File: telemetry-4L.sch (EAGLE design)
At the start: 70 parts, among them SW1 MF-SW-TACT-4.2MM, SW2 PCM12SMTR, U1 ATSAMD21G18A-MUT, U2 SPX3819M5-L-3-0, U3 MCP73831T-2ACI/OT, U4 IRLML6344TRPBF, U5 SIM868, U6 BMP280, U7 MPU-9250, U8 TPS61253YFFR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

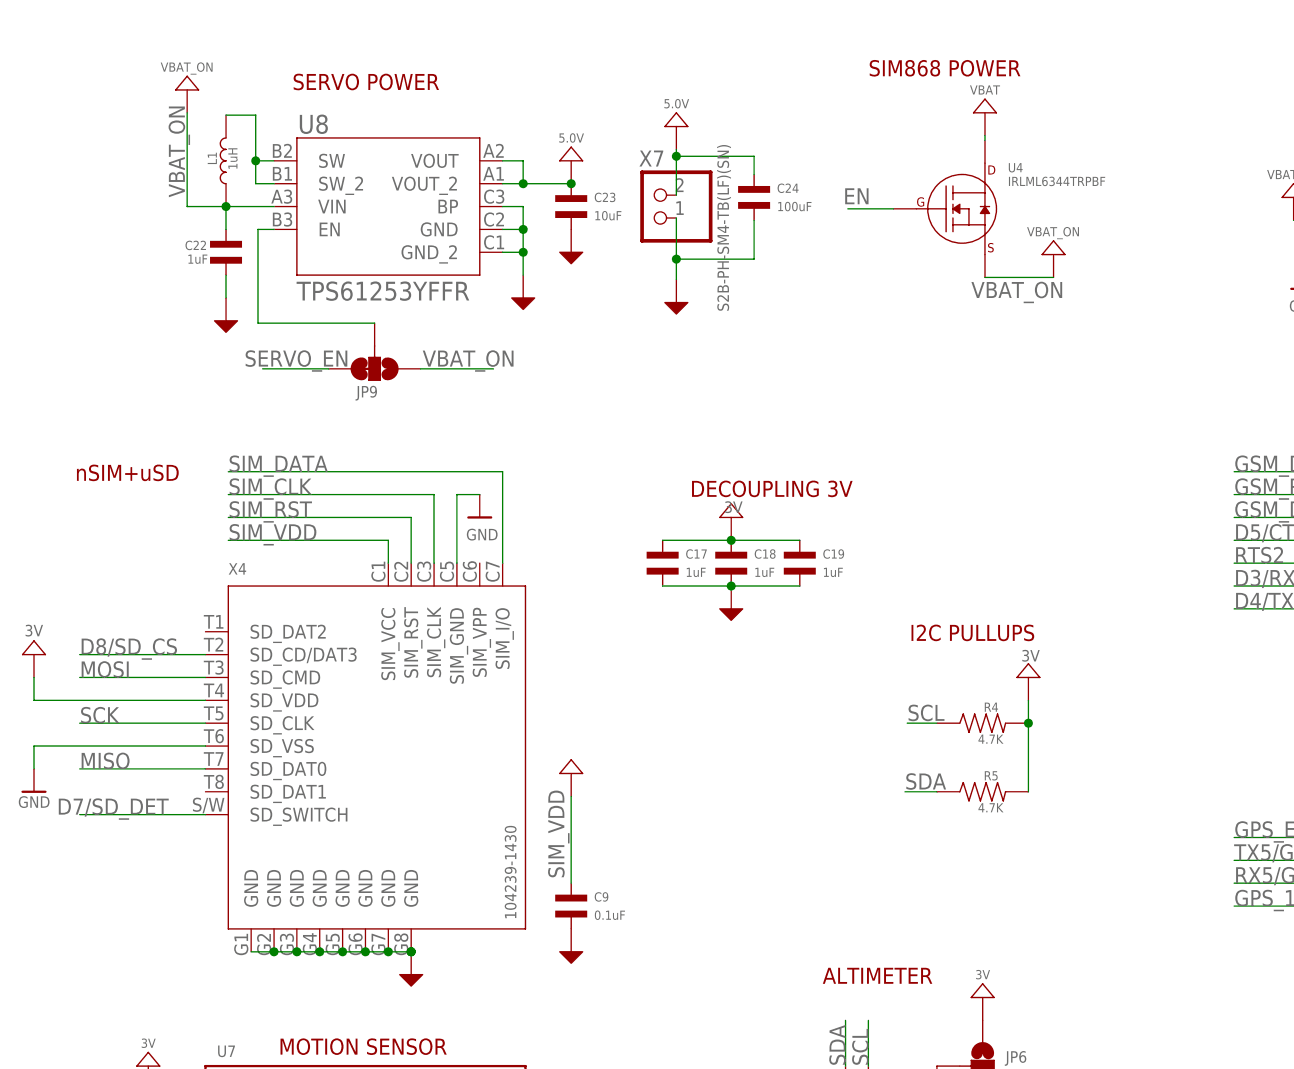
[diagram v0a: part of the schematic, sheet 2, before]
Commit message: Added a pull-down to 5V enable signal
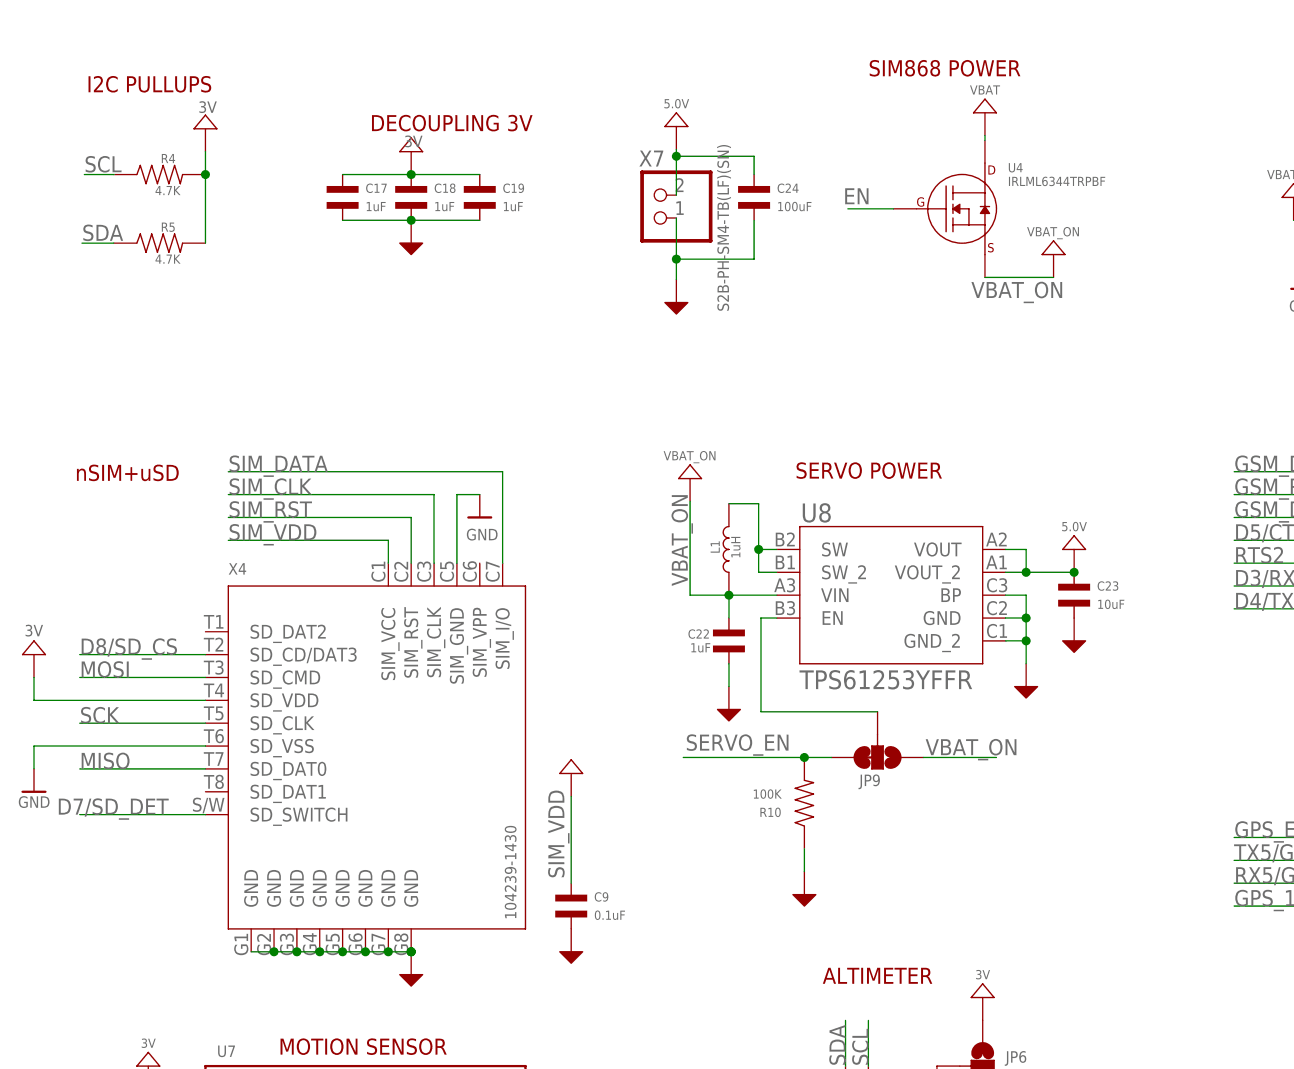
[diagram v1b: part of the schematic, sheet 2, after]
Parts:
- added R10: 100K, MF_Passives:RESISTOR_0402
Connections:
- removed net P$1: JP3.1
- net GND: now also R10.P$1
- net SERVO_EN: now also R10.P$2
- net VBAT_ON: now also JP3.1
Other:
- moved on the sheet: C17, C18, C19, C22, C23, JP9, L1, R4, R5, U8

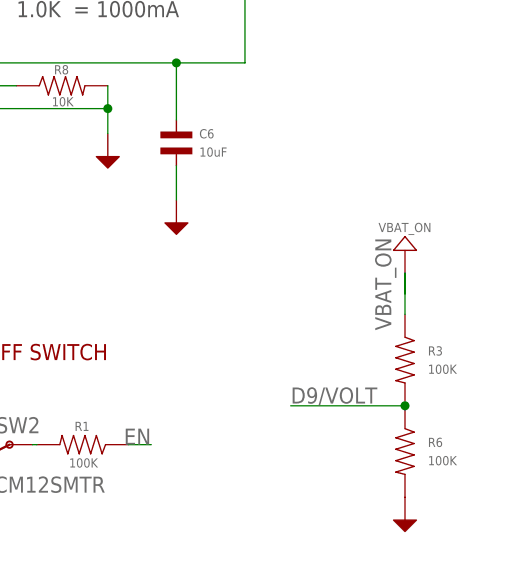
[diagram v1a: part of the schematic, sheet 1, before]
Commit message: fixed some unconnected airwires (important fix)
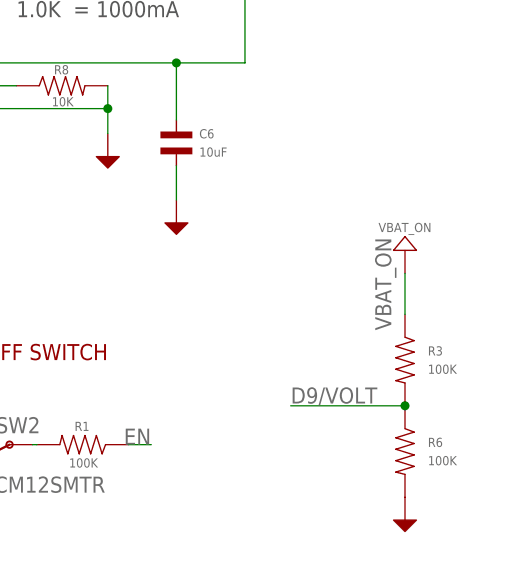
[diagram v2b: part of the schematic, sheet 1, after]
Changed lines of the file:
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@@
 </part>
 <part name="R10" library="MF_Passives" deviceset="RESISTOR" device="_0402" value="100K"/>
-<part name="U$61" library="MF_Aesthetics" deviceset="GND_RAIL" device=""/>
+<part name="GND" library="MF_Aesthetics" deviceset="GND_RAIL" device=""/>
 </parts>
 <sheets>
@@
 <label x="244.856" y="117.602" size="1.778" layer="95" rot="R90"/>
 <pinref part="U$59" gate="G$1" pin="P$1"/>
-<wire x1="246.38" y1="123.952" x2="246.38" y2="121.666" width="0.1524" layer="91"/>
 </segment>
 <segment>
@@
 <instance part="C24" gate="G$1" x="88.9" y="152.4"/>
 <instance part="R10" gate="G$1" x="94.488" y="85.09" rot="R180"/>
-<instance part="U$61" gate="G$1" x="94.488" y="74.93"/>
+<instance part="GND" gate="G$1" x="94.488" y="74.93"/>
 </instances>
 <busses>
@@
 <segment>
 <pinref part="R10" gate="G$1" pin="P$1"/>
-<pinref part="U$61" gate="G$1" pin="P$1"/>
+<pinref part="GND" gate="G$1" pin="P$1"/>
 <wire x1="94.488" y1="77.47" x2="94.488" y2="80.01" width="0.1524" layer="91"/>
 </segment>

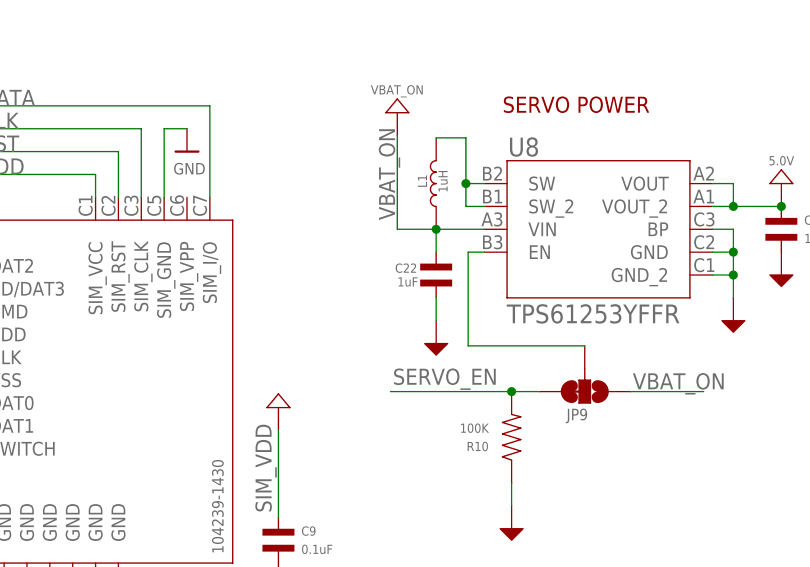
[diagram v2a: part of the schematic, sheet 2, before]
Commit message: Input capacitor for 5V regulator was wrong value
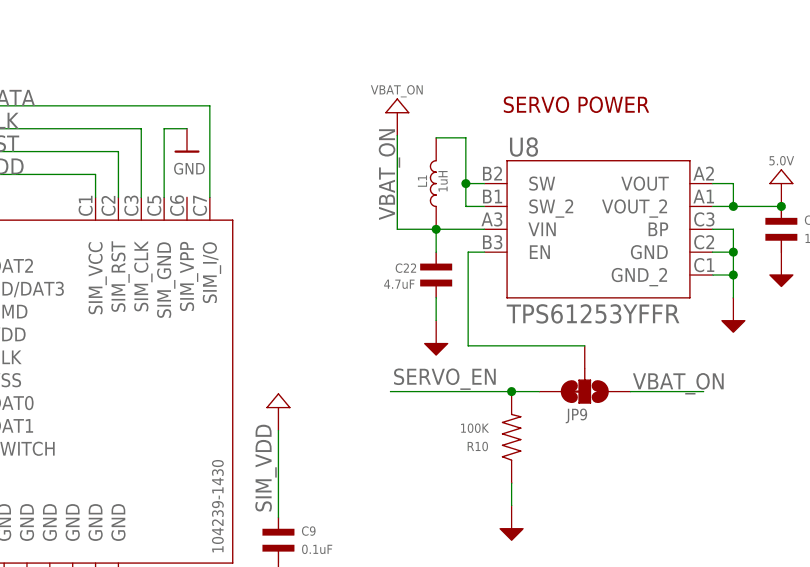
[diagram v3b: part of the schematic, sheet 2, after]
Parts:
- C22: value 1uF -> 4.7uF
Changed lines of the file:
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@@
 <attribute name="MPN" value="1277AS-H-1R0M=P2"/>
 </part>
-<part name="C22" library="MF_Passives" deviceset="CAPACITOR_NP" device="_0402" value="1uF"/>
+<part name="C22" library="MF_Passives" deviceset="CAPACITOR_NP" device="_0402" value="4.7uF"/>
 <part name="U$2" library="MF_Aesthetics" deviceset="GND_RAIL" device=""/>
 <part name="C23" library="MF_Passives" deviceset="CAPACITOR_NP" device="_0603" value="10uF">
@@
 <instance part="C22" gate="G$1" x="86.106" y="103.124" smashed="yes">
 <attribute name="NAME" x="81.534" y="104.394" size="1.016" layer="95" font="vector" align="top-left"/>
-<attribute name="VALUE" x="81.788" y="101.854" size="1.016" layer="96" font="vector"/>
+<attribute name="VALUE" x="80.264" y="101.6" size="1.016" layer="96" font="vector"/>
 </instance>
 <instance part="U$2" gate="G$1" x="86.106" y="95.504"/>

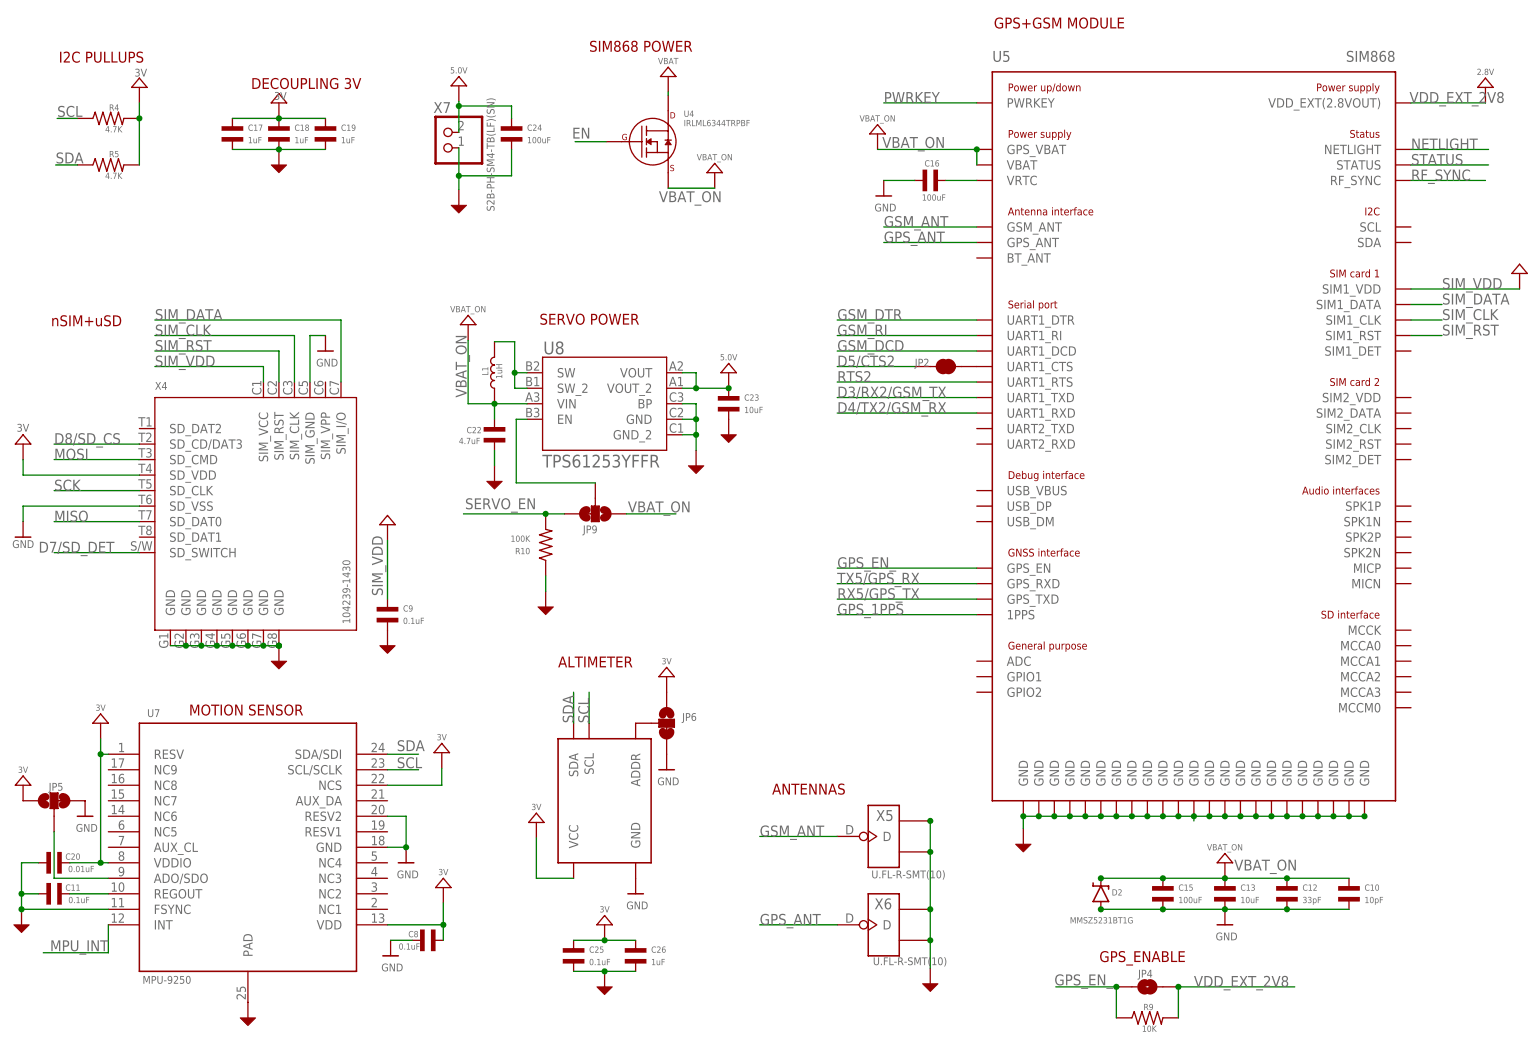
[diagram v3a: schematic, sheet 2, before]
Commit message: Added wind-down resistor to 5V output Killed cutout under MPU, as I don't know if it will work
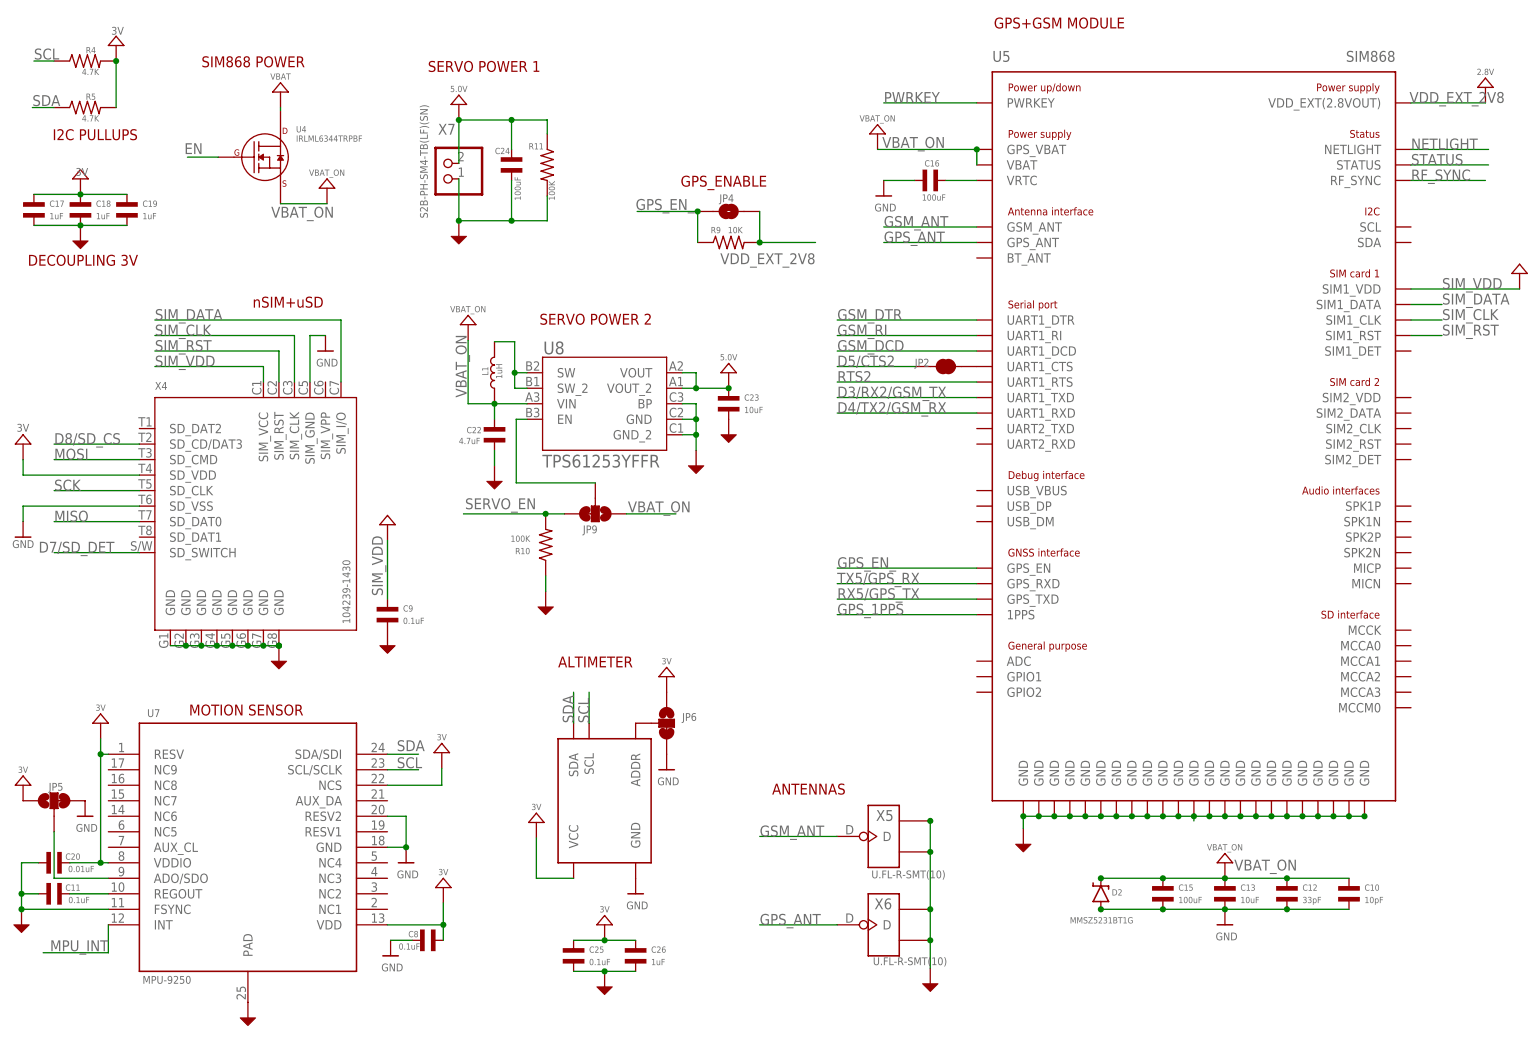
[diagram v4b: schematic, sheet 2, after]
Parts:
- added R11: 100K, MF_Passives:RESISTOR_0402
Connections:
- net 5.0V: now also R11.P$1
- net GND: now also R11.P$2
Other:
- note added: "SERVO POWER 1"
- note added: "SERVO POWER 2"
- note removed: "SERVO POWER"
- moved on the sheet: C17, C18, C19, C24, JP4, R4, R5, R9, U4, X7

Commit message: Small fixes
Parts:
- C22: MPN (none) -> GRM155R60J475ME47D
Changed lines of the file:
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@@
 <attribute name="MPN" value="1277AS-H-1R0M=P2"/>
 </part>
-<part name="C22" library="MF_Passives" deviceset="CAPACITOR_NP" device="_0402" value="4.7uF"/>
+<part name="C22" library="MF_Passives" deviceset="CAPACITOR_NP" device="_0402" value="4.7uF">
+<attribute name="MPN" value="GRM155R60J475ME47D"/>
+</part>
 <part name="U$2" library="MF_Aesthetics" deviceset="GND_RAIL" device=""/>
 <part name="C23" library="MF_Passives" deviceset="CAPACITOR_NP" device="_0603" value="10uF">

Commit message: added resistor to ground on DTR, as per SIM800 Serial App Note
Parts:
- added R12: 10K, MF_Passives:RESISTOR_0402
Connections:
- net GND: now also R12.P$1
- net GSM_DTR: now also R12.P$2
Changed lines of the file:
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@@
 <attribute name="MPN" value="SIM868"/>
 </part>
-<part name="U$37" library="microbuilder" deviceset="GND" device=""/>
 <part name="+3V6" library="MF_Aesthetics" deviceset="POWER_RAIL" device="" value="3V"/>
 <part name="X6" library="Seeed-Connector -2016" deviceset="ANTENNA-CONN-U-FL(3P)" device="" value="U.FL-R-SMT(10)"/>
@@
 <part name="GND" library="MF_Aesthetics" deviceset="GND_RAIL" device=""/>
 <part name="R11" library="MF_Passives" deviceset="RESISTOR" device="_0402" value="100K"/>
+<part name="R12" library="MF_Passives" deviceset="RESISTOR" device="_0402" value="10K"/>
+<part name="U$37" library="MF_Aesthetics" deviceset="GND_RAIL" device=""/>
+<part name="U$61" library="MF_Aesthetics" deviceset="GND_RAIL" device=""/>
 </parts>
 <sheets>
@@
 <attribute name="MPN" x="200.66" y="93.98" size="1.778" layer="96" display="off"/>
 </instance>
-<instance part="U$37" gate="G$1" x="149.86" y="142.24"/>
 <instance part="+3V6" gate="G$1" x="24.13" y="166.878" smashed="yes" rot="MR0">
 <attribute name="VALUE" x="25.4" y="168.656" size="1.27" layer="96" rot="MR0"/>
@@
 <attribute name="VALUE" x="96.012" y="141.478" size="1.016" layer="96" font="vector" rot="R90"/>
 </instance>
+<instance part="R12" gate="G$1" x="137.16" y="121.92" smashed="yes" rot="R90">
+<attribute name="NAME" x="138.176" y="123.444" size="1.016" layer="95" font="vector" rot="R180" align="top-left"/>
+<attribute name="VALUE" x="138.43" y="120.396" size="1.016" layer="96" font="vector" rot="R180"/>
+</instance>
+<instance part="U$37" gate="G$1" x="130.556" y="119.38"/>
+<instance part="U$61" gate="G$1" x="149.86" y="142.24"/>
 </instances>
 <busses>
@@
 <nets>
 <net name="GND" class="0">
-<segment>
-<pinref part="U$37" gate="G$1" pin="GND"/>
-<pinref part="C16" gate="G$1" pin="P$1"/>
-<wire x1="154.94" y1="144.78" x2="149.86" y2="144.78" width="0.1524" layer="91"/>
-</segment>
 <segment>
 <pinref part="X6" gate="G$1" pin="GND1"/>
@@
 <wire x1="94.488" y1="77.47" x2="94.488" y2="80.01" width="0.1524" layer="91"/>
 </segment>
+<segment>
+<pinref part="C16" gate="G$1" pin="P$1"/>
+<wire x1="154.94" y1="144.78" x2="149.86" y2="144.78" width="0.1524" layer="91"/>
+<pinref part="U$61" gate="G$1" pin="P$1"/>
+</segment>
+<segment>
+<pinref part="R12" gate="G$1" pin="P$1"/>
+<wire x1="130.556" y1="121.92" x2="132.08" y2="121.92" width="0.1524" layer="91"/>
+<pinref part="U$37" gate="G$1" pin="P$1"/>
+</segment>
 </net>
 <net name="SCL" class="0">
@@
 <wire x1="142.24" y1="121.92" x2="165.1" y2="121.92" width="0.1524" layer="91"/>
 <label x="142.24" y="121.92" size="1.778" layer="95"/>
-</segment>
-</net>
+<pinref part="R12" gate="G$1" pin="P$2"/>
+</segment>
+</net>
